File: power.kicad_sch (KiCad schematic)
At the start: 45 parts, among them J2 B3B-XH-A, U5 EG11752, U6 BQ25606RGER, U9 ME6211C33M5G

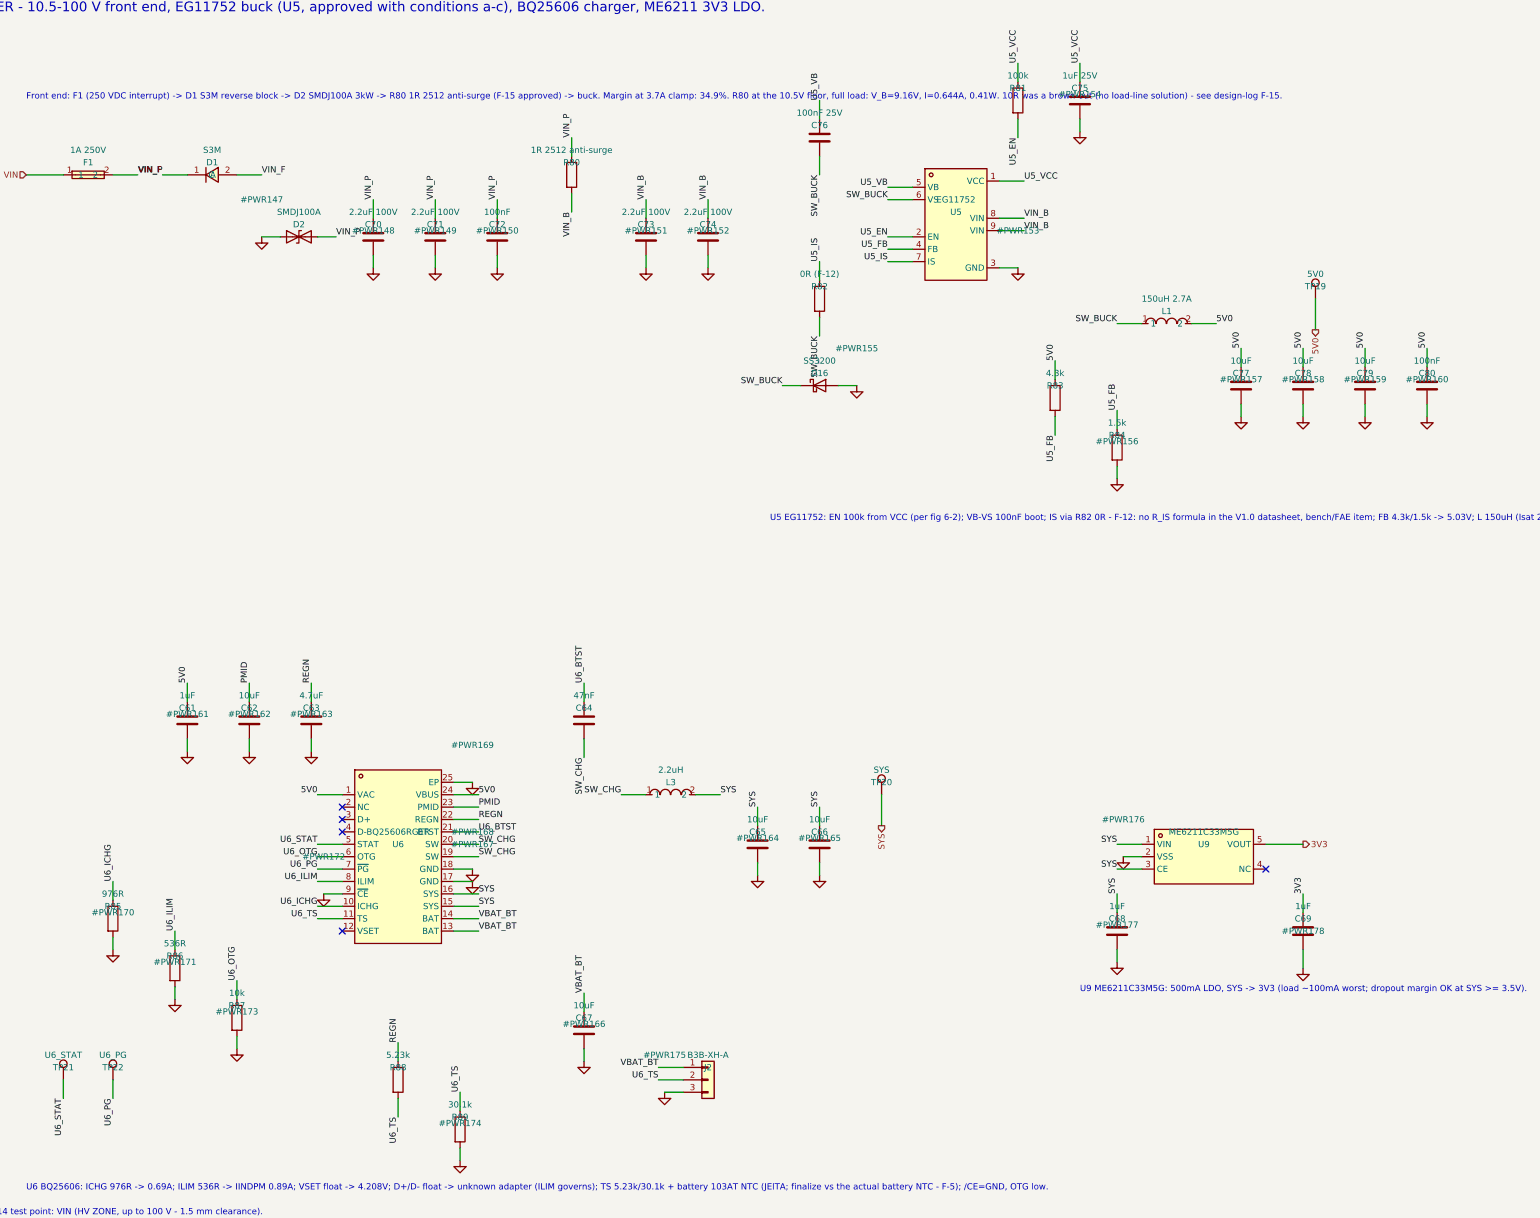
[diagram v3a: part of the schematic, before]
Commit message: M4 stage 2: F-13, F-16, F-17 closed; full placement + planes (NOT routed)
F-13 APPLIED (no waiver): VBAT_MODEM bulk 2x 100uF 6.3V X5R (C49066, which
broke rule 1 twice - X5R, and 6.3/4.35 = 1.45:1 not >=2:1) -> 4x 47uF 10V X7R
Murata GRM32ER71A476KE15L (C84494), refs C40/C41/C81/C82. 27.97uF per part read
at exact 4.35V/85.0C grid points from Murata's simulation backend = 111.9uF
effective, 2.30:1 derating. Cross-validated within ~7% by Taiyo Yuden C20486249
(second source). 10uF X5R 0805 -> C109040 X7S, +125C rated. Rule 1 now MET.
Also logged: all three previously-recorded F-13 options actually deliver only
63/76/92uF; no 100uF X7R/X7S >=10V exists in 1210/1812 from anyone; and
multiplying a 25C bias curve by a 0V temperature curve over-predicts by 9-12%.

F-17 CLOSED: derived lib/jlc.pretty/eSIM_MFF2_VFDFPN8.kicad_mod from four
independent vendor documents that publish an identical land, plus normative
ETSI TS 102 671 V12.0.0. ETSI table 6.1 confirms the schematic pinout is
correct (pins 1-8 = C5,C6,C7,C8,C4,C3,C2,C1). EP tied to GND per Infineon p.24
and numbered "1" so it merges with the GND pin. Logged as a deliberate
golden-rule-1 deviation: MFF2 is a package site, not an LCSC part, so there is
no C-number to import. This was the last unresolved footprint and the only
footprint_link_issues warning, so ERC is now 0 errors / 13 warnings.

F-16: X ambiguity RESOLVED - the incumbent's 8.50 is post-to-post centres, and
the earlier reading of 2.50/1.22 as post positions was wrong (they are the
bottom-pad chain). Y remains genuinely ambiguous. Three vendors (GCT, HRO,
Megastar) publish an identical scheme giving Y = +1.25; GCT's numbers were
re-extracted and verified locally. Megastar C7419882 (+13%) is fully
dimensioned BUT easyeda2kicad has no data for it, so switching means a
hand-drawn footprint - held for the user rather than trading a verified
imported footprint for a documented hand-drawn one. SIM area reserved with the
incumbent pad map and NO post holes, so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
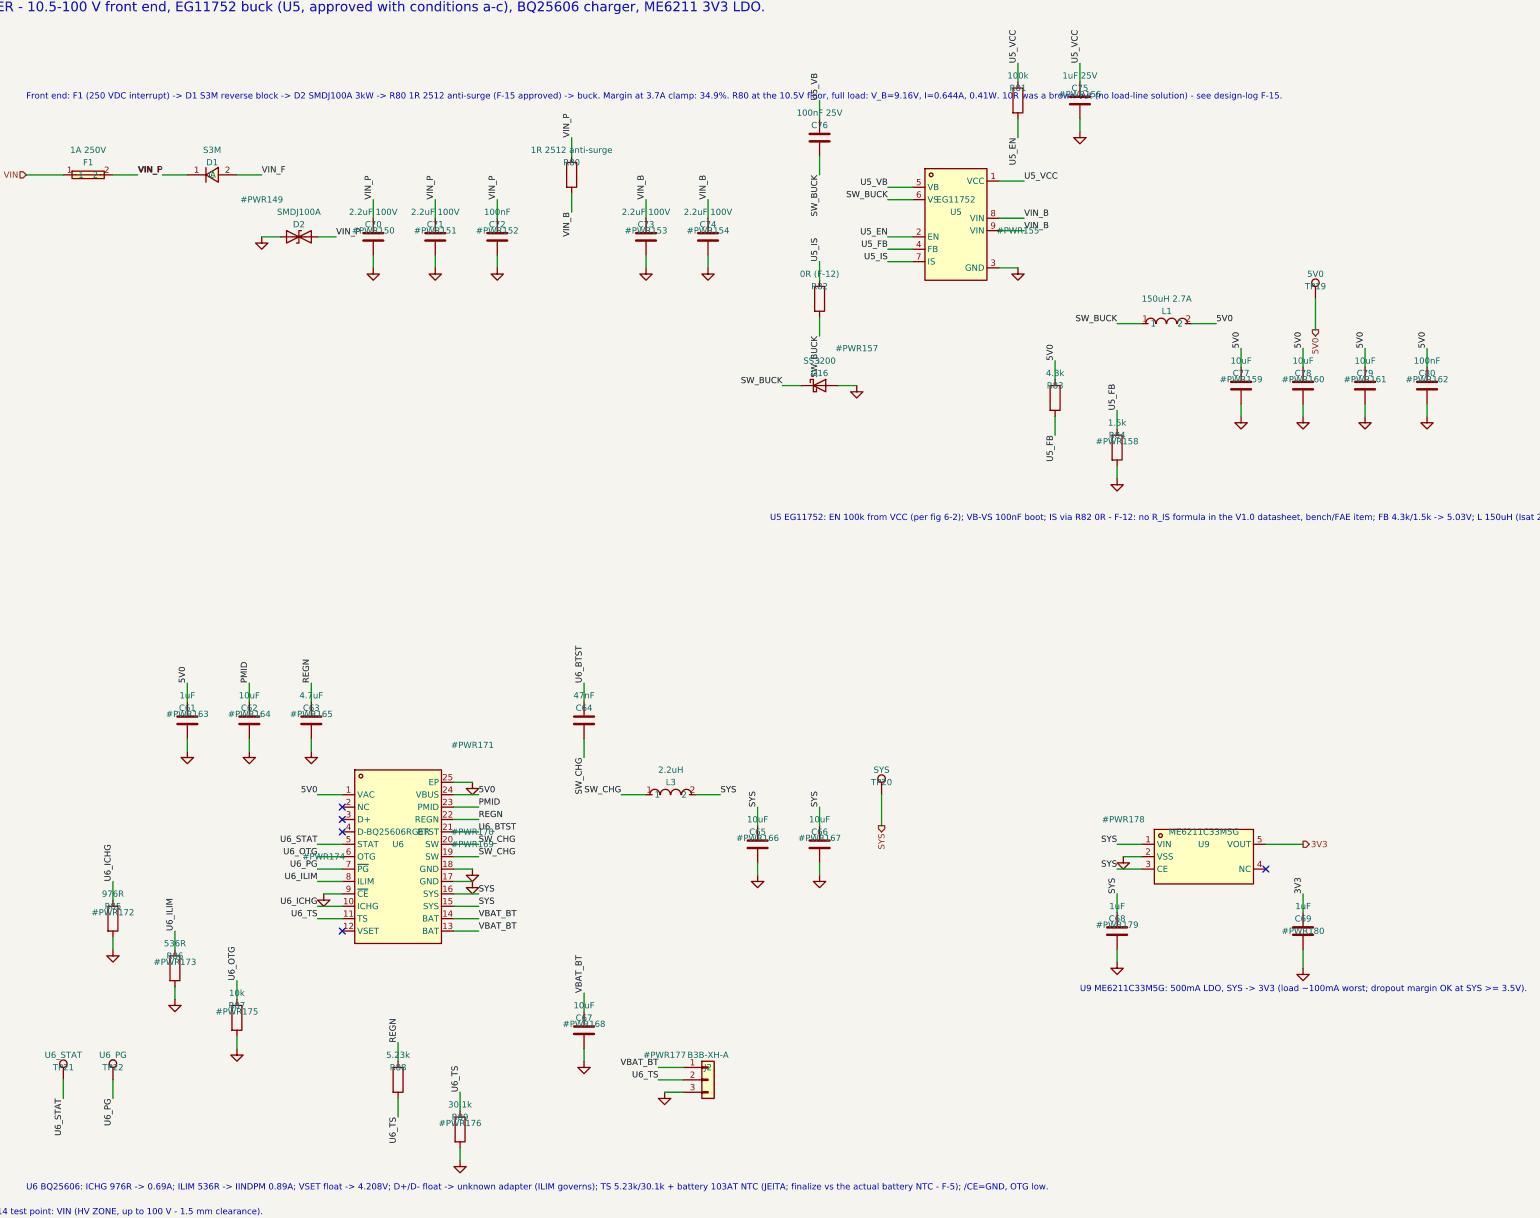
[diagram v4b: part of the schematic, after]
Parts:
- C62, C65, C66, C67, C77, C78, C79: LCSC C440198 -> C109040

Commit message: GNSS bias-T (DNP) per Quectel fig 31; check 2 reclassified; log 7-of-8
ANT_GNSS pin 47 is AI, 50 ohm, with NO internal DC feed (Table 37 p.67), so an
external bias-T is correct. Quectel figure 31 (p.68) is itself the reference
bias-T and its values are what the schematic now uses: L4 47nH series, C84
100pF shunt, R90 10R + C83 100nF on the 3V3 feed, all DNP - note 2 says the
VDD circuit is not needed for a passive antenna.

NEW FLAG F-21: Quectel's figure DC-couples the module pin to the injection node
through the 0R, so 3V3 would sit on ANT_GNSS with the bias-T fitted. The R72
position is documented 0R-or-DC-block. Do not populate until settled.

Check 2 reclassified as instructed: PCB copper keepout is N/A because both
antennas are lid-mounted and reach the board only by U.FL pigtail; the
metal-clearance figure becomes an installation/housing requirement. Still FAIL
pending antenna selection. Fixed a checker false positive - R80's value
'1R 2512 anti-surge' contains the substring ANT.

ERC 0/13, checkpins exit 0, DRC 19 + 452 unconnected.

Co-Authored-By: Claude Opus 5 (1M context) <noreply@anthropic.com>
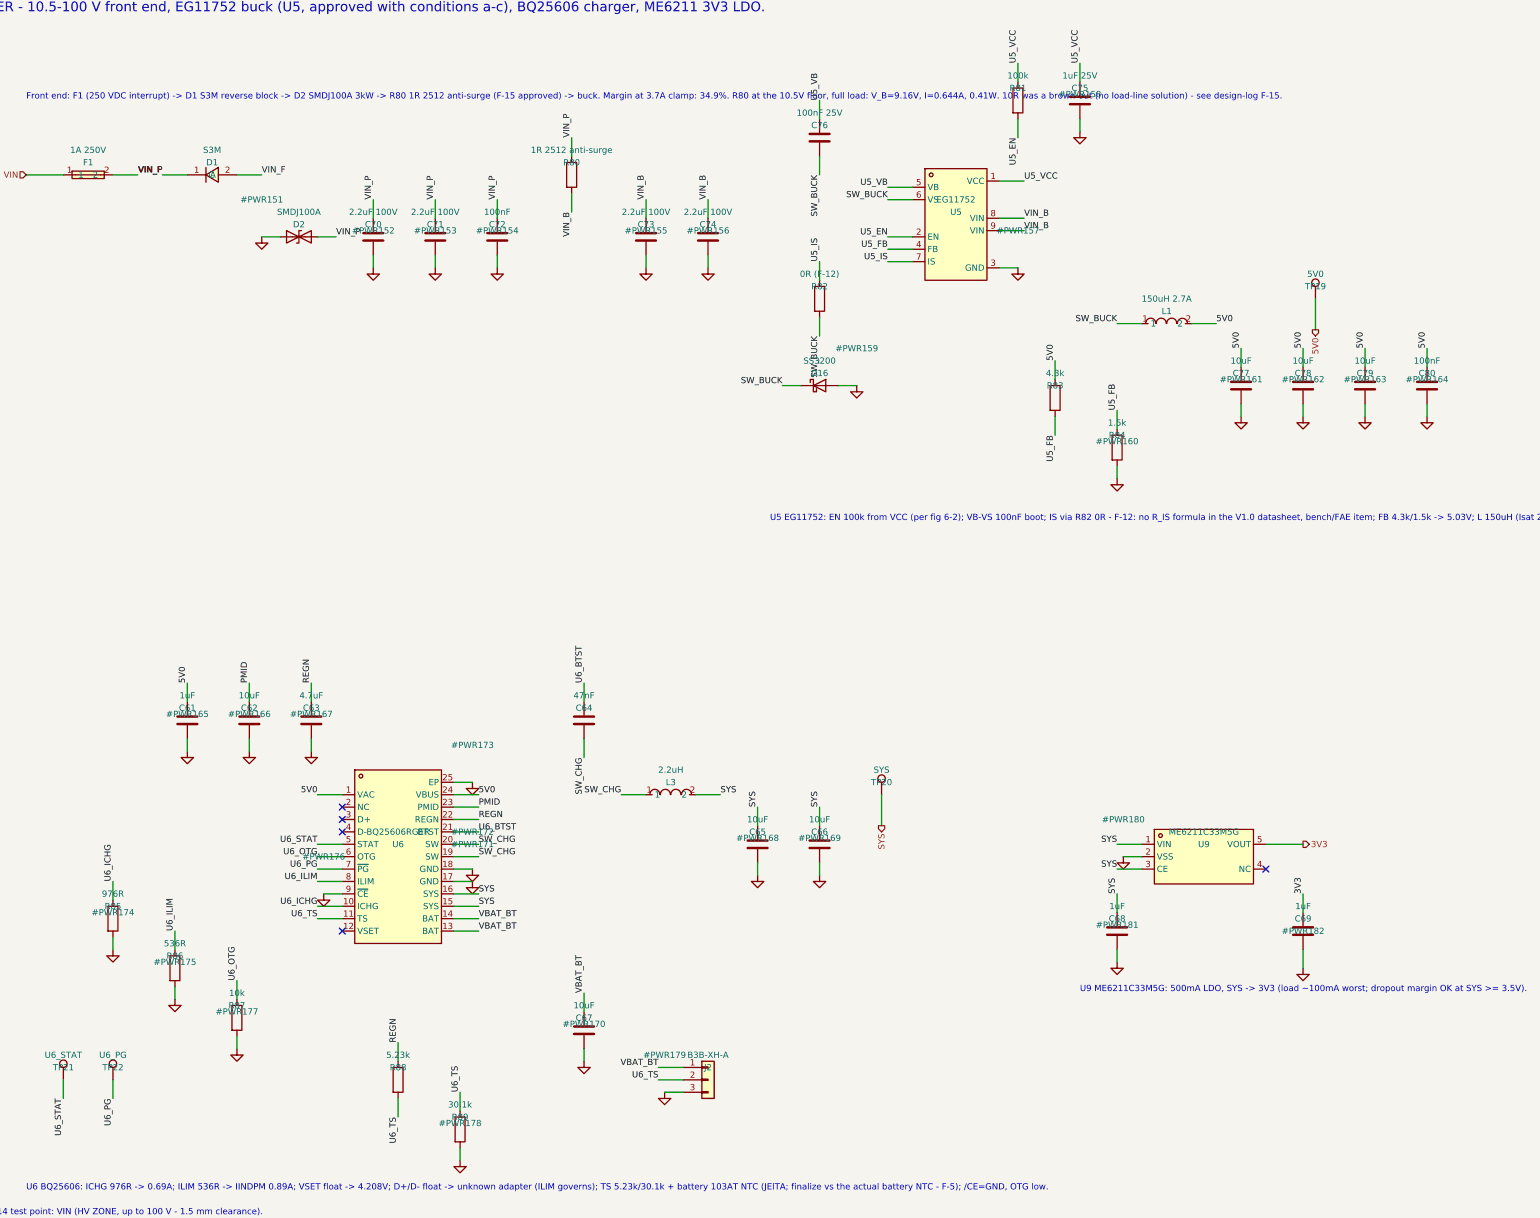
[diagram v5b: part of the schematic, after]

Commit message: F-21 RETRACTED (my misread); antennas selected; 8 of 8 floorplan checks pass
F-21 was wrong and the error was mine. I read the pdftotext -layout dump, where
0R and 100 pF share a row and NM NM sit below, and took the 100 pF for a shunt.
Rendering page 69 at 200 dpi shows it has VERTICAL plates in the signal line: it
is a SERIES DC BLOCK, and the 47 nH injects VDD on the ANTENNA side of it. The
module pin is DC-isolated by construction; there was never a conflict.
Corroborated by Antenna Design Guide V3.3 5.1 note 5, which also asks for
>= 56 nH - so L4 is 68 nH, not figure 31's 47 nH. Table 40 does not list
ANT_GNSS at all, so there is no published DC rating for pin 47, which is the
real reason the block is mandatory.

Schematic corrected: C84 100 pF is in SERIES and ALWAYS FITTED (depopulating it
opens the antenna; 1.0 ohm at 1575 MHz). Only L4/R90/C83 are DNP. Chain verified
in the netlist: U1.47 -> R72 -> C84 -> AF2.3, bias injected at ANT_GNSS_F.
C84 anchored inline in the RF corridor and check 1 extended to validate every
inline element. checkpins caught a real short while doing this - the first
bias-T placement merged GNSS_BIAS into USIM_VDD.

Parts: C1546 100pF C0G (always fitted), C3221844 Murata LQW15AN68NG80D 68 nH
WIREWOUND SRF 2.5 GHz (every multilayer 0402 at this value has SRF ~1.1 GHz and
is capacitive at 1575 MHz), C25077 10R, C60474 0.1uF.

Antennas: LTE C496569 Bat Wireless BW4GFNX39-15B1, 700-2700 MHz continuous,
120 mm IPEX-1 pigtail, 5536 stock. Runner-up C22467619 rejected - it omits B40,
which Jio uses heavily in India.

GNSS C784386 - but this is a DEVIATION NEEDING A DECISION: no passive 25x25
patch with a U.FL pigtail exists in LCSC stock, so the recommendation is ACTIVE
(LNA 21.5 dB, 1.8-3.6 V, 4.3 mA). That makes the bias-T MANDATORY rather than
DNP for the internal build. Passive alternative C784398 has solder pins and no
cable, needing a hand-added pigtail and a 60-70 mm lid ground plane.

Quectel's < 17 dB LNA limit is a recommendation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
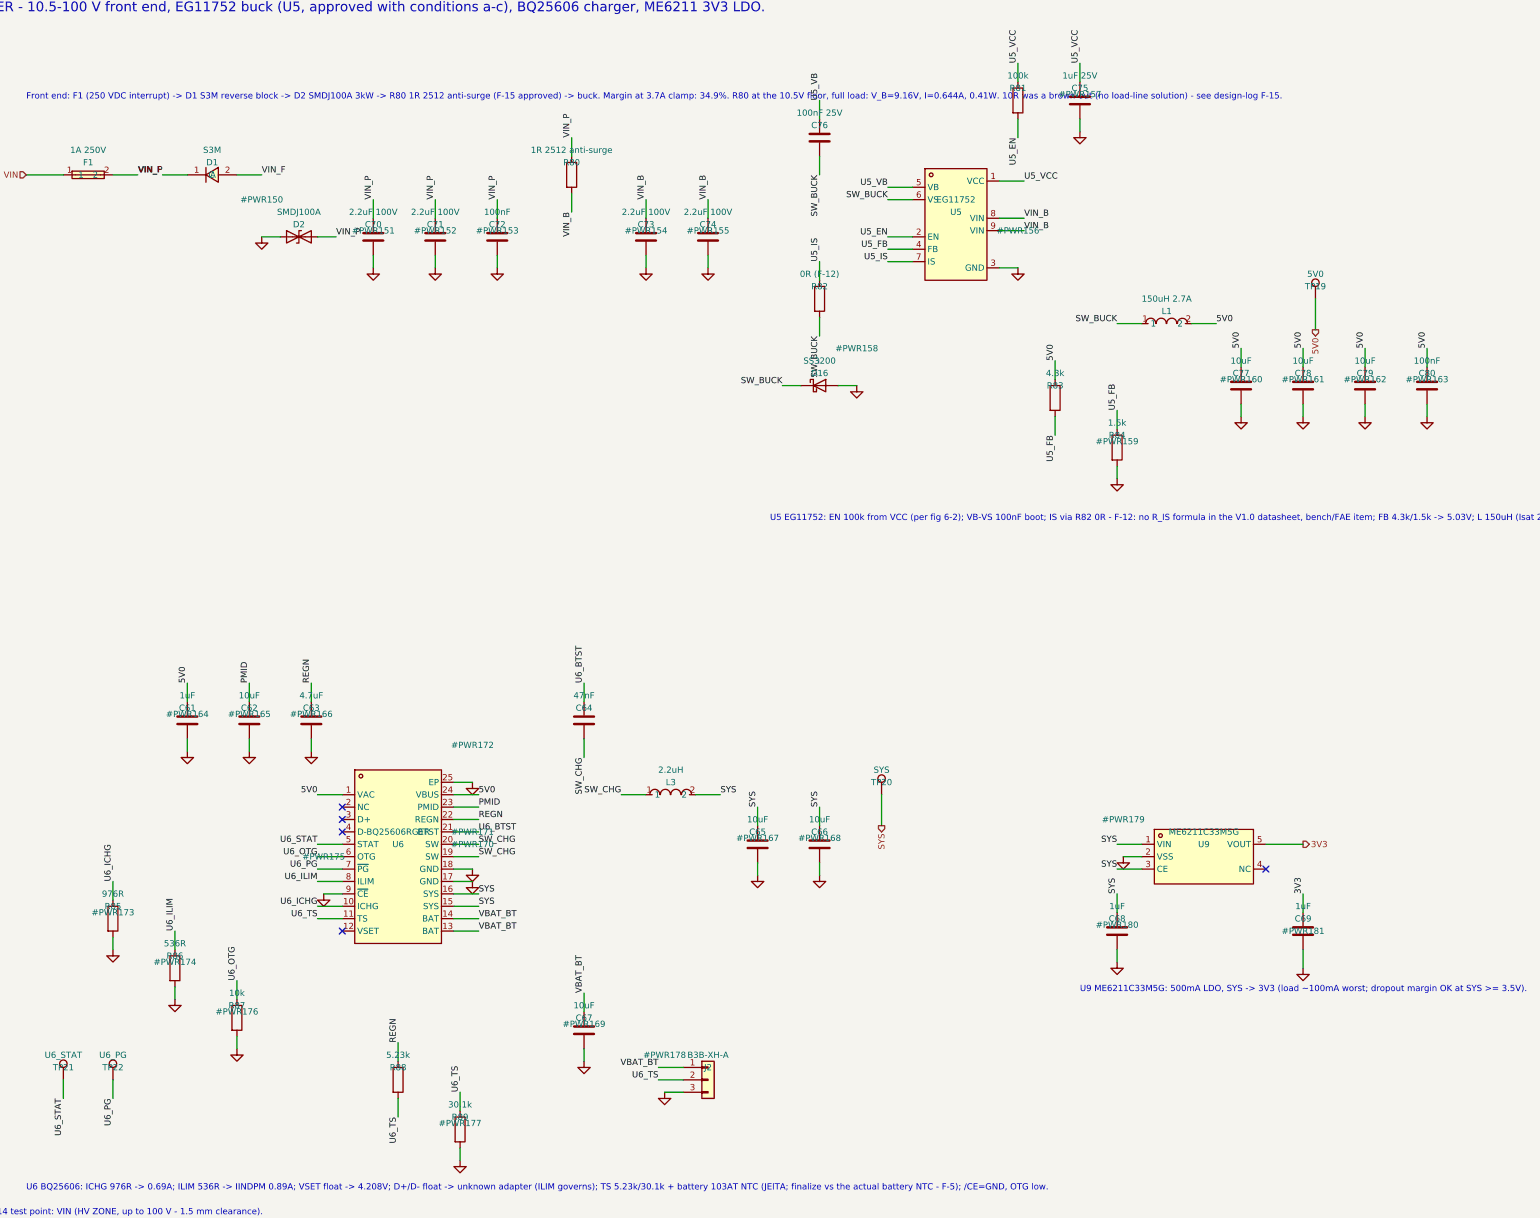
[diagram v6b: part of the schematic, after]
